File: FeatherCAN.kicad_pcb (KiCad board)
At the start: 2 copper layers, 50.8 x 22.9 mm, 32 parts, among them J1 feather long, J2 feather short, J3 Header, J4 PicoBlade, U1 DS3231MZ, U2 MCP2515-xST, U3 MCP2551-I-SN, U4 5V, Y1 16MHz

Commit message: first version sent for production review
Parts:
- added G***: LOGO, tunaf1sh/JBR-logos.pretty:jbr-binary-xs-mask, F.Cu at (135.2, 100.1)
- added G***: LOGO, tunaf1sh/JBR-logos.pretty:jbr_logo_sm, B.Cu at (139.5, 106.0)
- D3: value Green -> PWR
- J1: value feather long -> Feather Long
- J2: value feather short -> Feather Short
- moved BT1 114.2 mm to (125.5, 103.9)
- moved J2 114.2 mm to (160.7, 95.9)
- moved J4 114.2 mm to (164.3, 106.0)
- moved R6 114.2 mm to (134.8, 104.5)
- moved REF** 114.2 mm to (164.5, 97.1)
- moved REF** 114.2 mm to (164.5, 114.9)
- moved U2 114.2 mm to (144.4, 109.0)
- moved C1 114.2 mm to (159.0, 112.5)
- moved C2 114.2 mm to (152.9, 111.6)
- moved C3 114.2 mm to (139.1, 103.1)
- moved C4 114.2 mm to (144.9, 103.1)
- moved C5 114.2 mm to (156.2, 102.6)
- moved C6 114.2 mm to (140.0, 107.0)
- moved D2 114.2 mm to (148.4, 100.1)
- moved D3 114.2 mm to (151.3, 111.6)
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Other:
- board text added: "4. GND 3. CANH 2. CANL 1. 5-16V"
- board text added: "FeatherCAN 1.0 J.Whittington 2019"
- board text added: "RTERM"

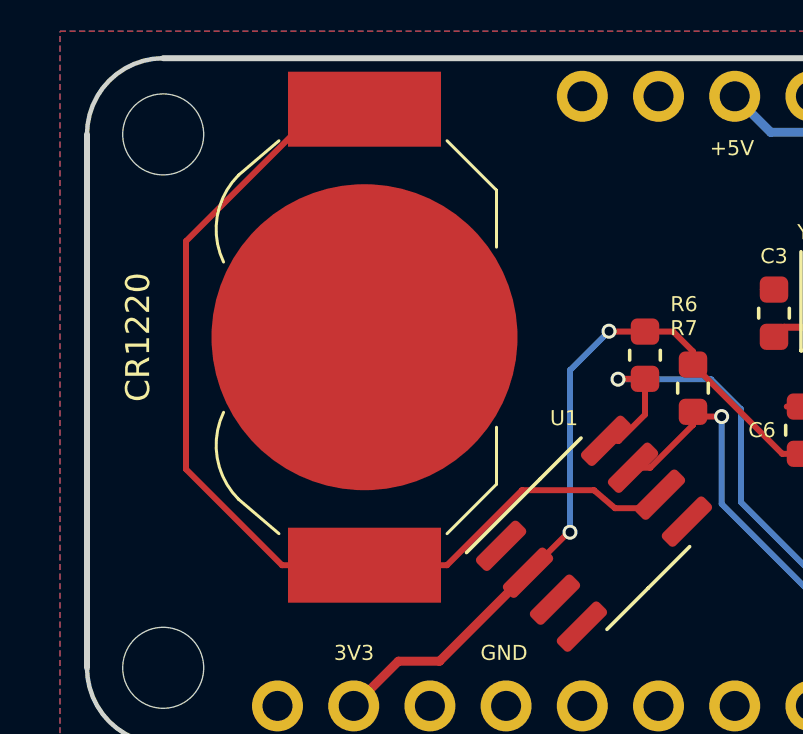
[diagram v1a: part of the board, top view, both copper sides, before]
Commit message: add README and silk logo
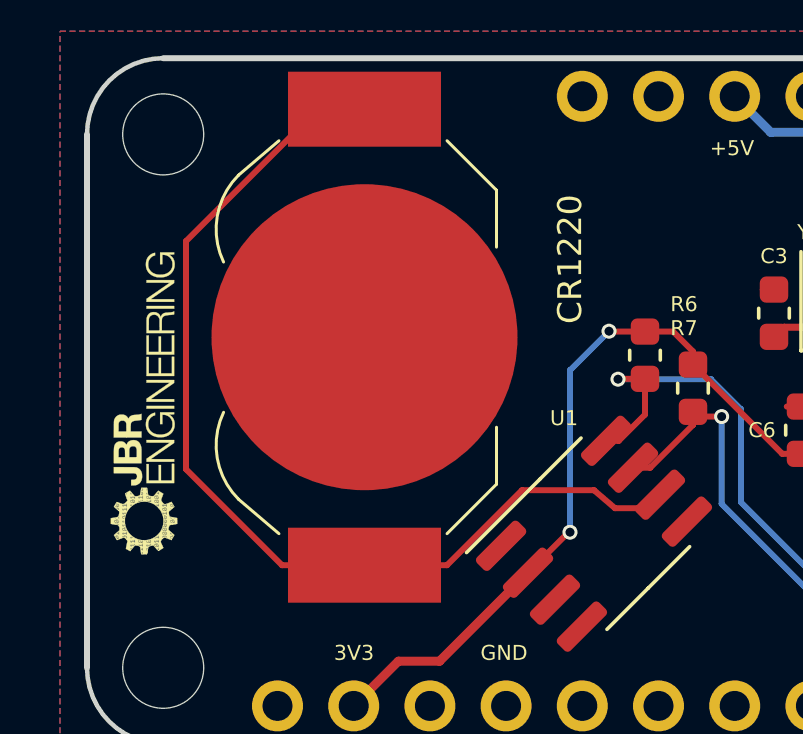
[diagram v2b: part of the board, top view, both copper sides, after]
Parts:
- removed the G*** at (139.5, 106.0)
- added G***: LOGO, tunaf1sh/JBR-logos.pretty:FeatherCAN, B.Cu at (140.1, 105.9)
- added G***: LOGO, tunaf1sh/JBR-logos.pretty:jbr_logo_tiny, F.Cu at (118.1, 106.1)
- added G***: LOGO, tunaf1sh/JBR-logos.pretty:jbr_logo_tiny, B.Cu at (118.1, 106.1)
- added G***: LOGO, tunaf1sh/JBR-logos.pretty:FeatherCAN, B.Cu at (131.2, 104.8)
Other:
- board text added: "*No connect VIN and VUSB at some time!"
- board text added: "1.0 - JBR Engineering 2019"
- board text added: "4. GND 3. CANH 2. CANL 1. 5-16V*"
- board text added: "FeatherCAN"
- board text removed: "4. GND 3. CANH 2. CANL 1. 5-16V"
- board text removed: "FeatherCAN 1.0 J.Whittington 2019"

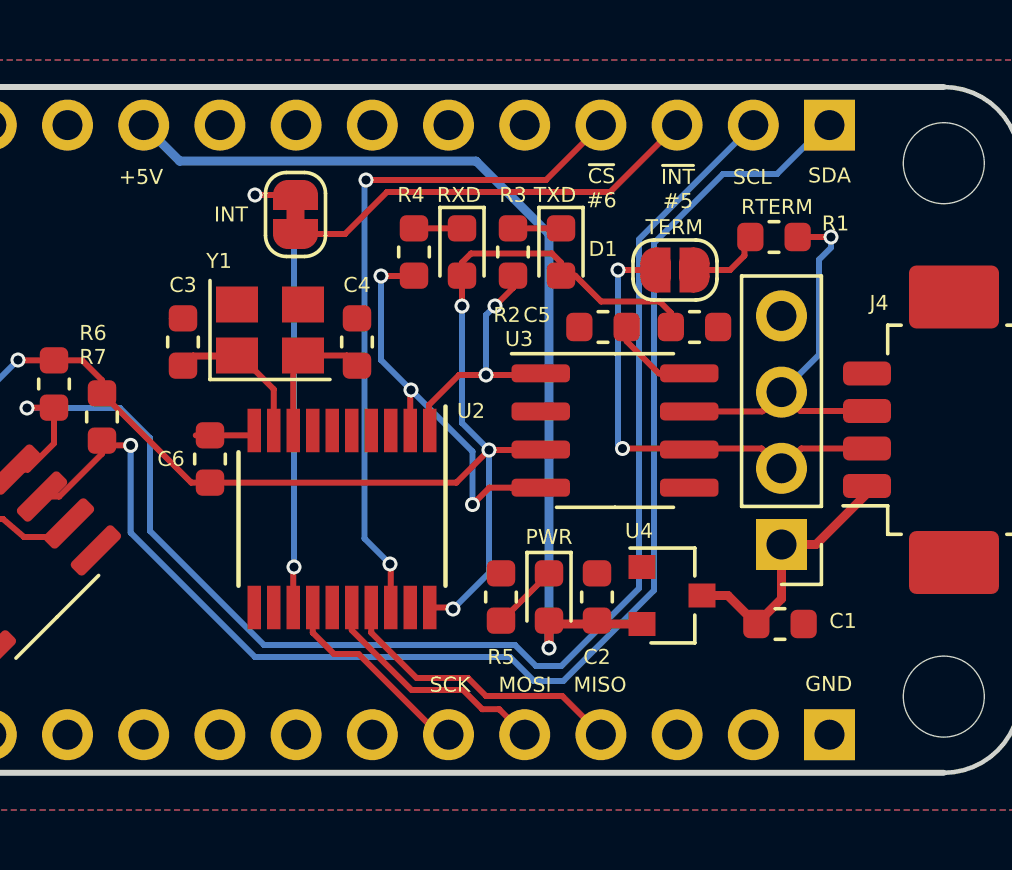
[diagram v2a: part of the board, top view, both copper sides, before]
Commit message: pull-up on MCP reset and fix 4-pad crystal pins
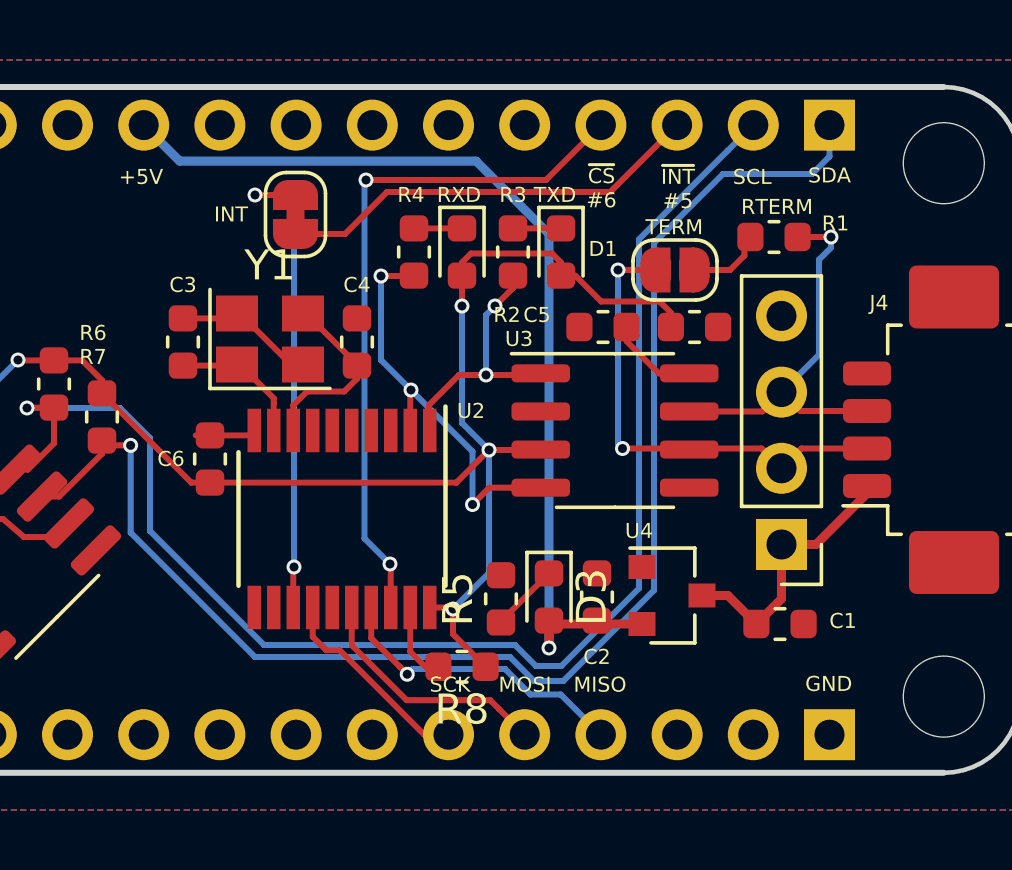
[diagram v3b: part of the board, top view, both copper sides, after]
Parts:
- added R8: 1k, KiCad/Resistor_SMD.pretty:R_0603_1608Metric, F.Cu at (148.4, 113.9)
- moved Y1 0.30 mm to (142.0, 103.0)
- moved R5 0.06 mm to (149.7, 111.7)
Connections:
- Y1 pad 2: Net-(C4-Pad2) -> GND
- Y1 pad 3: (no net) -> Net-(C4-Pad2)
- Y1 pad 4: (no net) -> GND
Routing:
- net GND: track 2.49 -> 7.26 mm
- net Net-(R8-Pad2): track 0.00 -> 2.62 mm
- net Net-(C3-Pad2): track 6.97 -> 4.58 mm
- net VCC: track 58.8 -> 61.2 mm
- net Net-(C4-Pad2): track 4.57 -> 6.31 mm
- net /SDA: track 46.9 -> 47.5 mm
- net /MISO: track 9.90 -> 10.2 mm, vias 0 -> 1

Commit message: add CAN transeiver lines for STM32 Feather peripheral
STM32 Feather has CAN RX/TX on #9 and #10. Can be cut if user wants to
use pins on other Feather.
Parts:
- added JP3: INT, KiCad/Jumper.pretty:SolderJumper-2_P1.3mm_Bridged_RoundedPad1.0x1.5mm, B.Cu at (149.8, 98.7)
- added JP4: INT, KiCad/Jumper.pretty:SolderJumper-2_P1.3mm_Bridged_RoundedPad1.0x1.5mm, B.Cu at (152.4, 98.7)
- moved JP1 0.20 mm to (155.5, 100.5)
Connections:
- J2 pad 5: Net-(J2-Pad5) -> /FC_RX
- J2 pad 6: Net-(J2-Pad6) -> /FC_TX
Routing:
- net Net-(JP4-Pad1): track 14.8 -> 26.8 mm, vias 3 -> 4
- net /FC_RX: track 0.00 -> 2.93 mm
- net /FC_TX: track 0.00 -> 2.92 mm
- net Net-(JP3-Pad1): track 8.71 -> 11.5 mm
- net +5V: track 32.9 -> 32.2 mm
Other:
- board text added: "1.1 - JBR Engineering 2019"
- board text removed: "1.0 - JBR Engineering 2019"

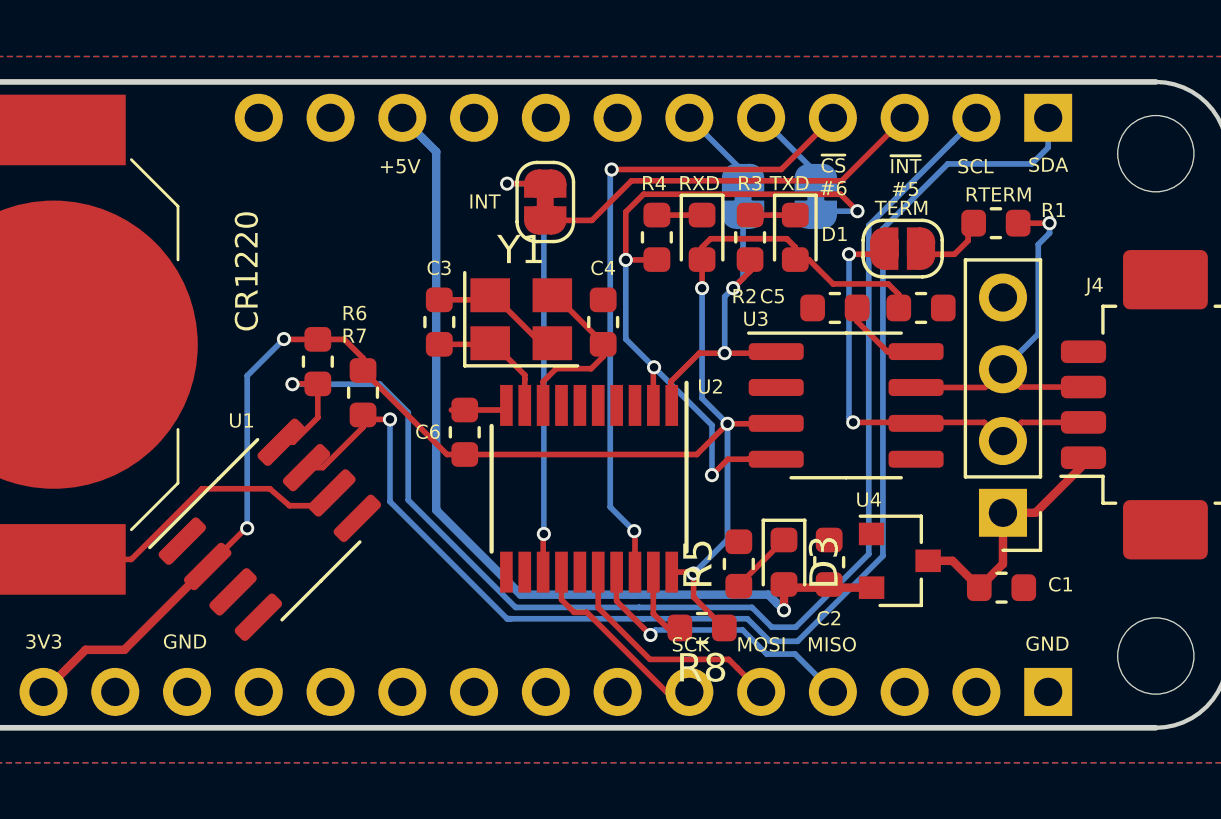
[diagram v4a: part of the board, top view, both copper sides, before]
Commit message: MCP2515 Vdd is +5 V
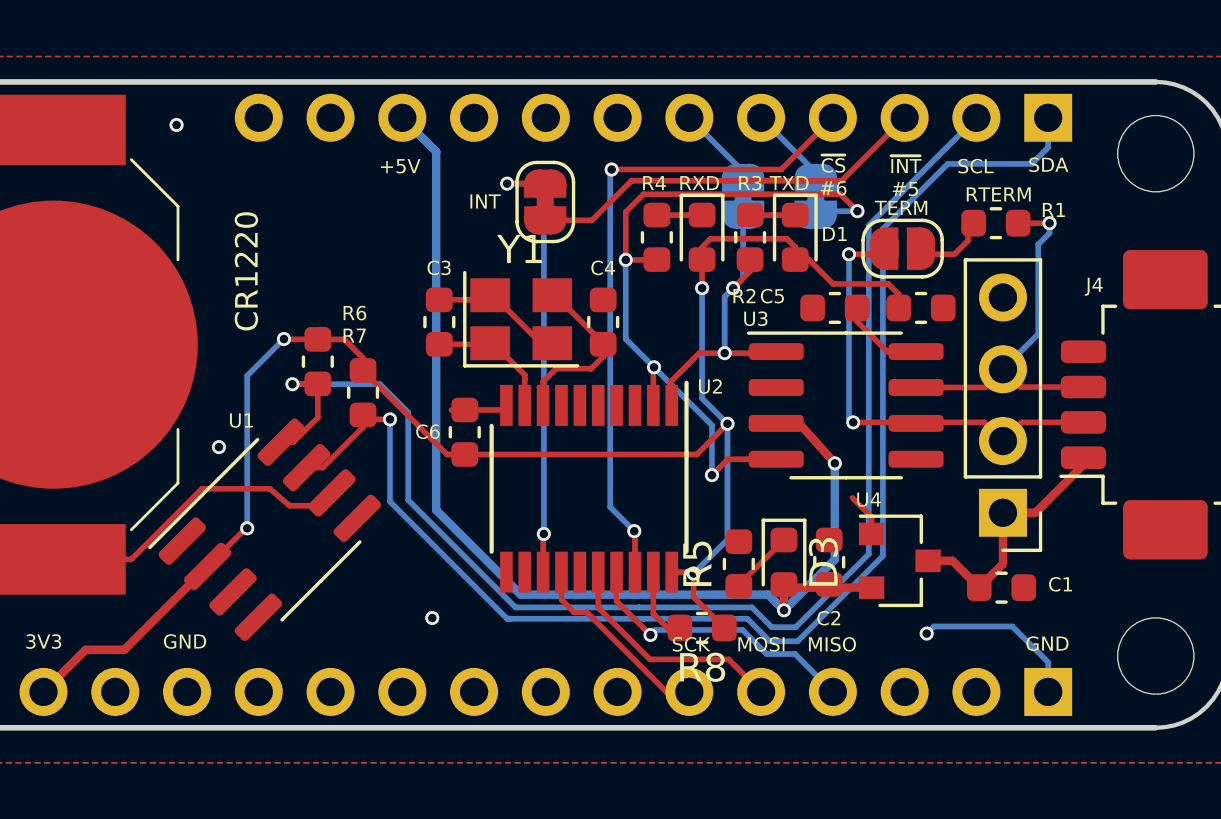
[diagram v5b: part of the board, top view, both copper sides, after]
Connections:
- U3 pad 3: VCC -> +5V
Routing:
- net +5V: track 32.2 -> 40.9 mm, vias 1 -> 2
- net GND: track 7.26 -> 14.8 mm, vias 0 -> 3
- net VCC: track 61.2 -> 59.5 mm
- net (no net): vias 0 -> 1

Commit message: gerbers and kitspcae
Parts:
- added D4: 40V 200mA, KiCad/Diode_SMD.pretty:D_0603_1608Metric, F.Cu at (159.1, 112.5)
- added G***: LOGO, tunaf1sh/JBR-logos.pretty:feathercan_ver, B.Cu at (133.8, 101.5)
- added TP1: RTC_BAT, KiCad/TestPoint.pretty:TestPoint_Pad_D2.5mm, B.Cu at (122.7, 111.3)
- JP3, JP4: footprint KiCad/Jumper.pretty:SolderJumper-2_P1.3mm_Bridged_RoundedPad1.0x1.5mm -> KiCad/Jumper.pretty:SolderJumper-2_P1.3mm_Open_RoundedPad1.0x1.5mm
- moved C1 1.58 mm to (159.0, 114.1)
- moved G*** 0.50 mm to (140.1, 106.4)
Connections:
- net Net-(BT1-Pad1) renamed +BATT
- C1 pad 1: /VIN -> Net-(C1-Pad1)
- U4 pad 3: /VIN -> Net-(C1-Pad1)
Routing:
- net Net-(C1-Pad1): track 0.00 -> 4.21 mm
- net /VIN: track 9.01 -> 6.76 mm
- net +BATT: track 33.9 -> 34.0 mm, vias 0 -> 1
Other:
- board text added: "#9/#10 CAN RX/TX"
- board text added: "~CS"
- board text added: "~INT"
- board text removed: "*No connect VIN and VUSB at some time!"
- board text removed: "1.1 - JBR Engineering 2019"
- board text removed: "FeatherCAN"
- board text removed: "~CS #6"
- board text removed: "~INT #5"

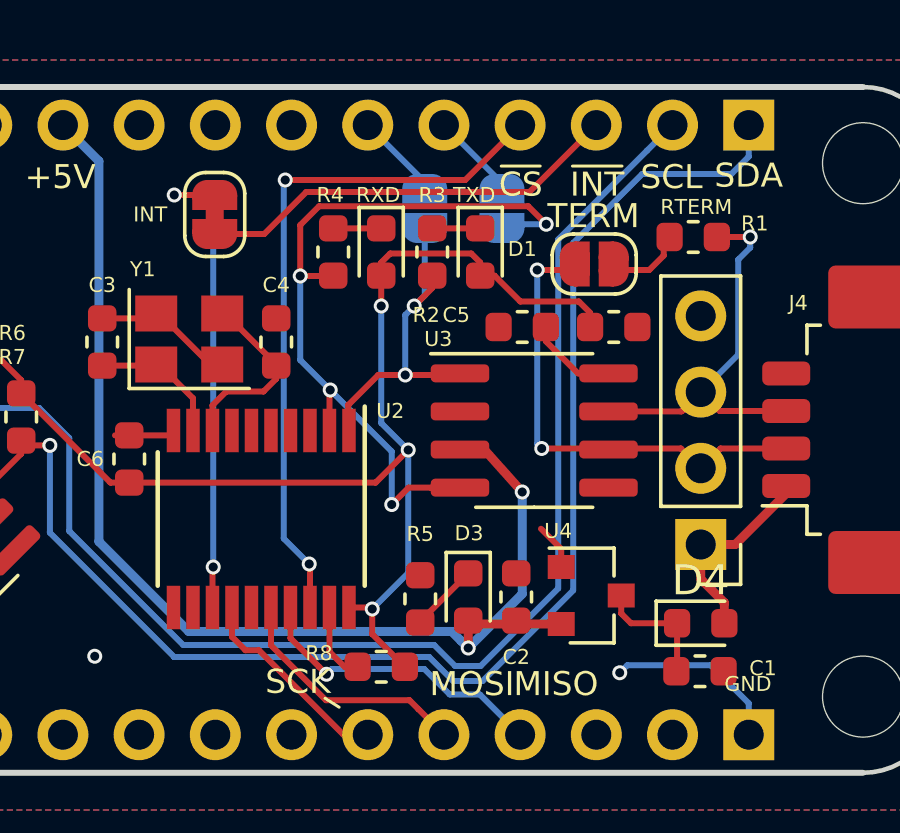
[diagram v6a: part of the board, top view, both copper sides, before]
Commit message: MCP2551 swap to SN65 for Vcc logic
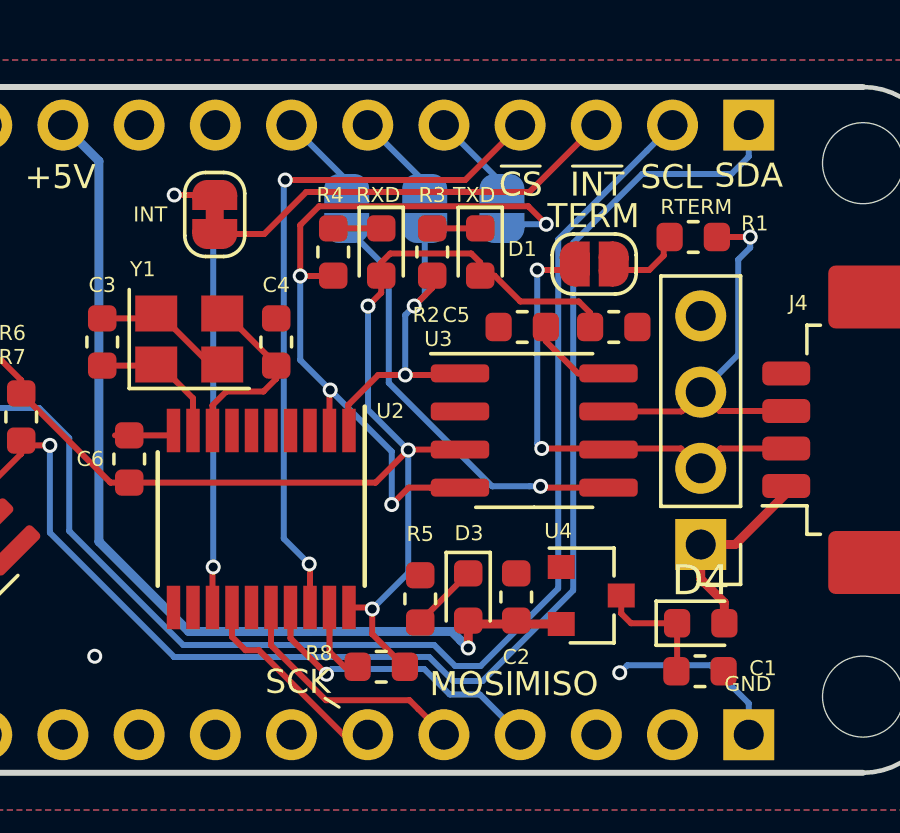
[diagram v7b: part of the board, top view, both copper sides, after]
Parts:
- added JP5: INT, KiCad/Jumper.pretty:SolderJumper-2_P1.3mm_Open_RoundedPad1.0x1.5mm, B.Cu at (147.2, 98.7)
- U3: value MCP2551-I-SN -> SN65HVD230
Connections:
- J2 pad 7: Net-(J2-Pad7) -> /FC_RS
- U3 pad 3: +5V -> VCC
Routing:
- net Net-(JP5-Pad1): track 0.00 -> 14.5 mm, vias 0 -> 1
- net +5V: track 40.9 -> 32.2 mm, vias 2 -> 1
- net /FC_RS: track 0.00 -> 2.89 mm
- net VCC: track 59.5 -> 61.6 mm
- net GND: track 14.8 -> 13.3 mm
